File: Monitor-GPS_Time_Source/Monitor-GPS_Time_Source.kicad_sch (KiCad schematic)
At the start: 17 parts, among them J1 Conn_ARM_JTAG_SWD_10, J2 Conn_01x10_Pin, J3 Conn_01x10_Pin, J4 Conn_01x03_Pin, SW2 SW_Push, U1 MSPM0C1105, U2 BL8565

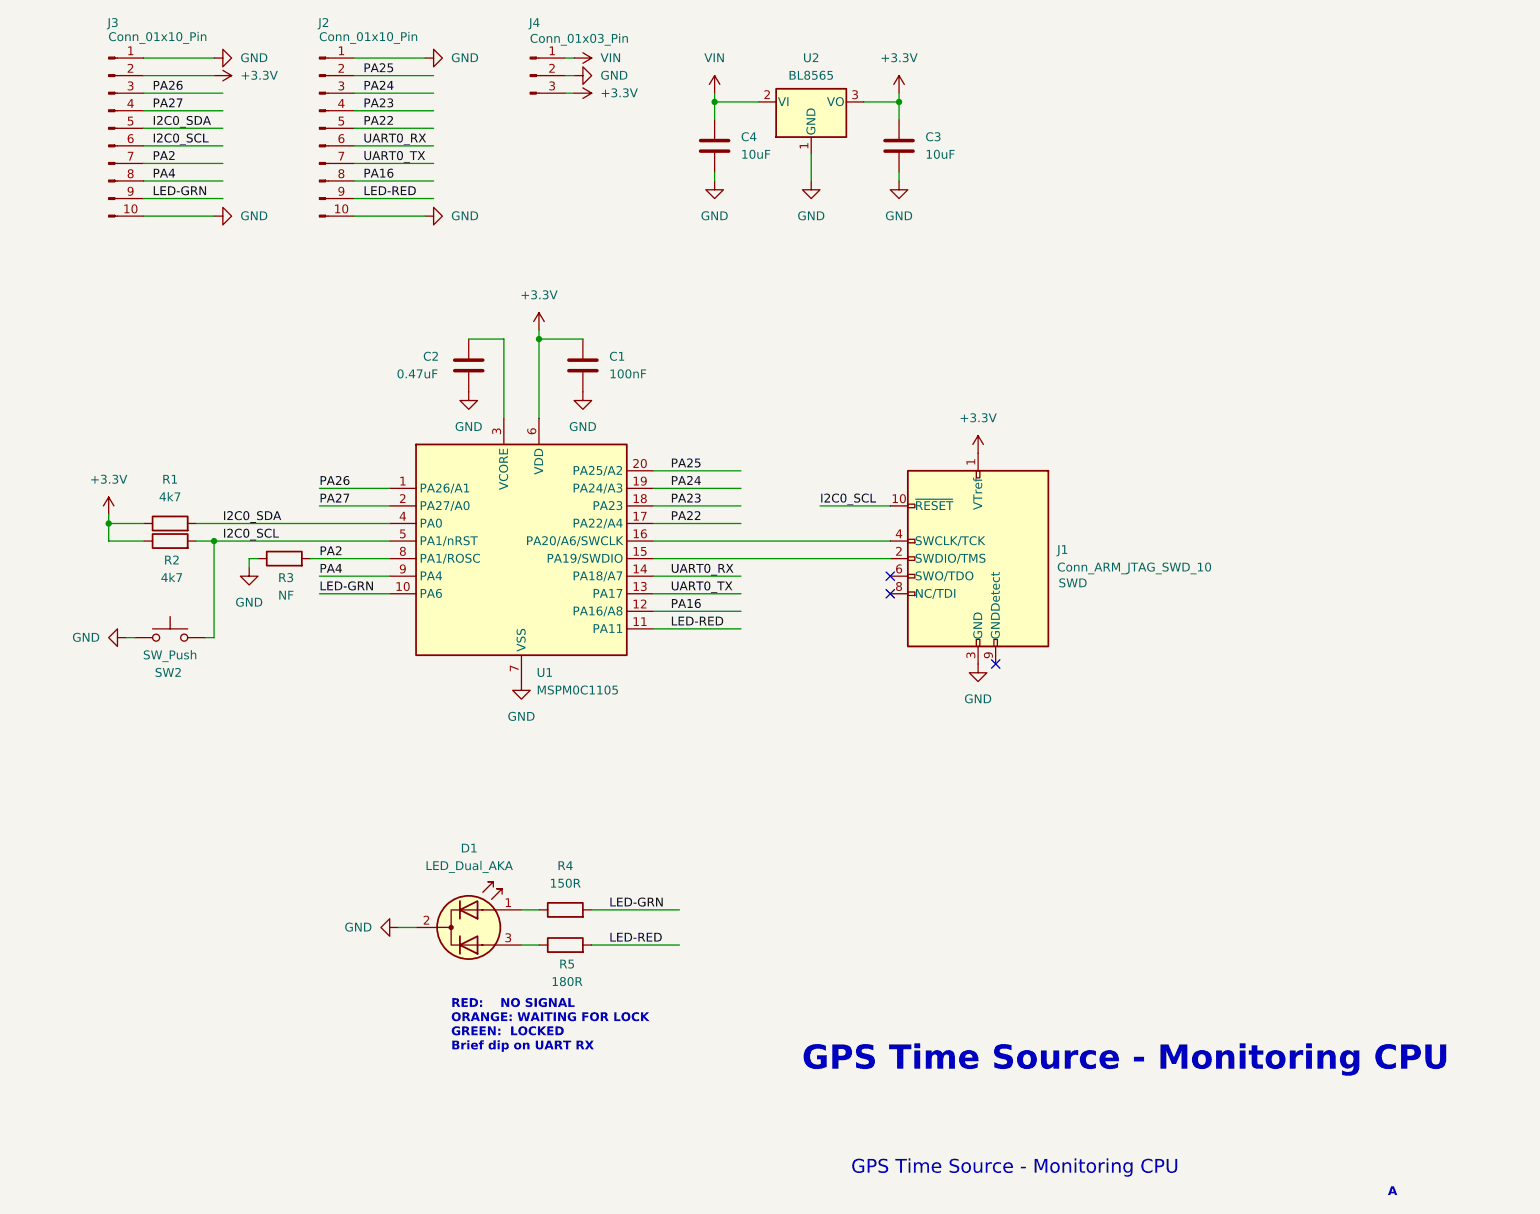
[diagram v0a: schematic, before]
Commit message: Add silkscreen text. Update sch to support MSPM0C110x
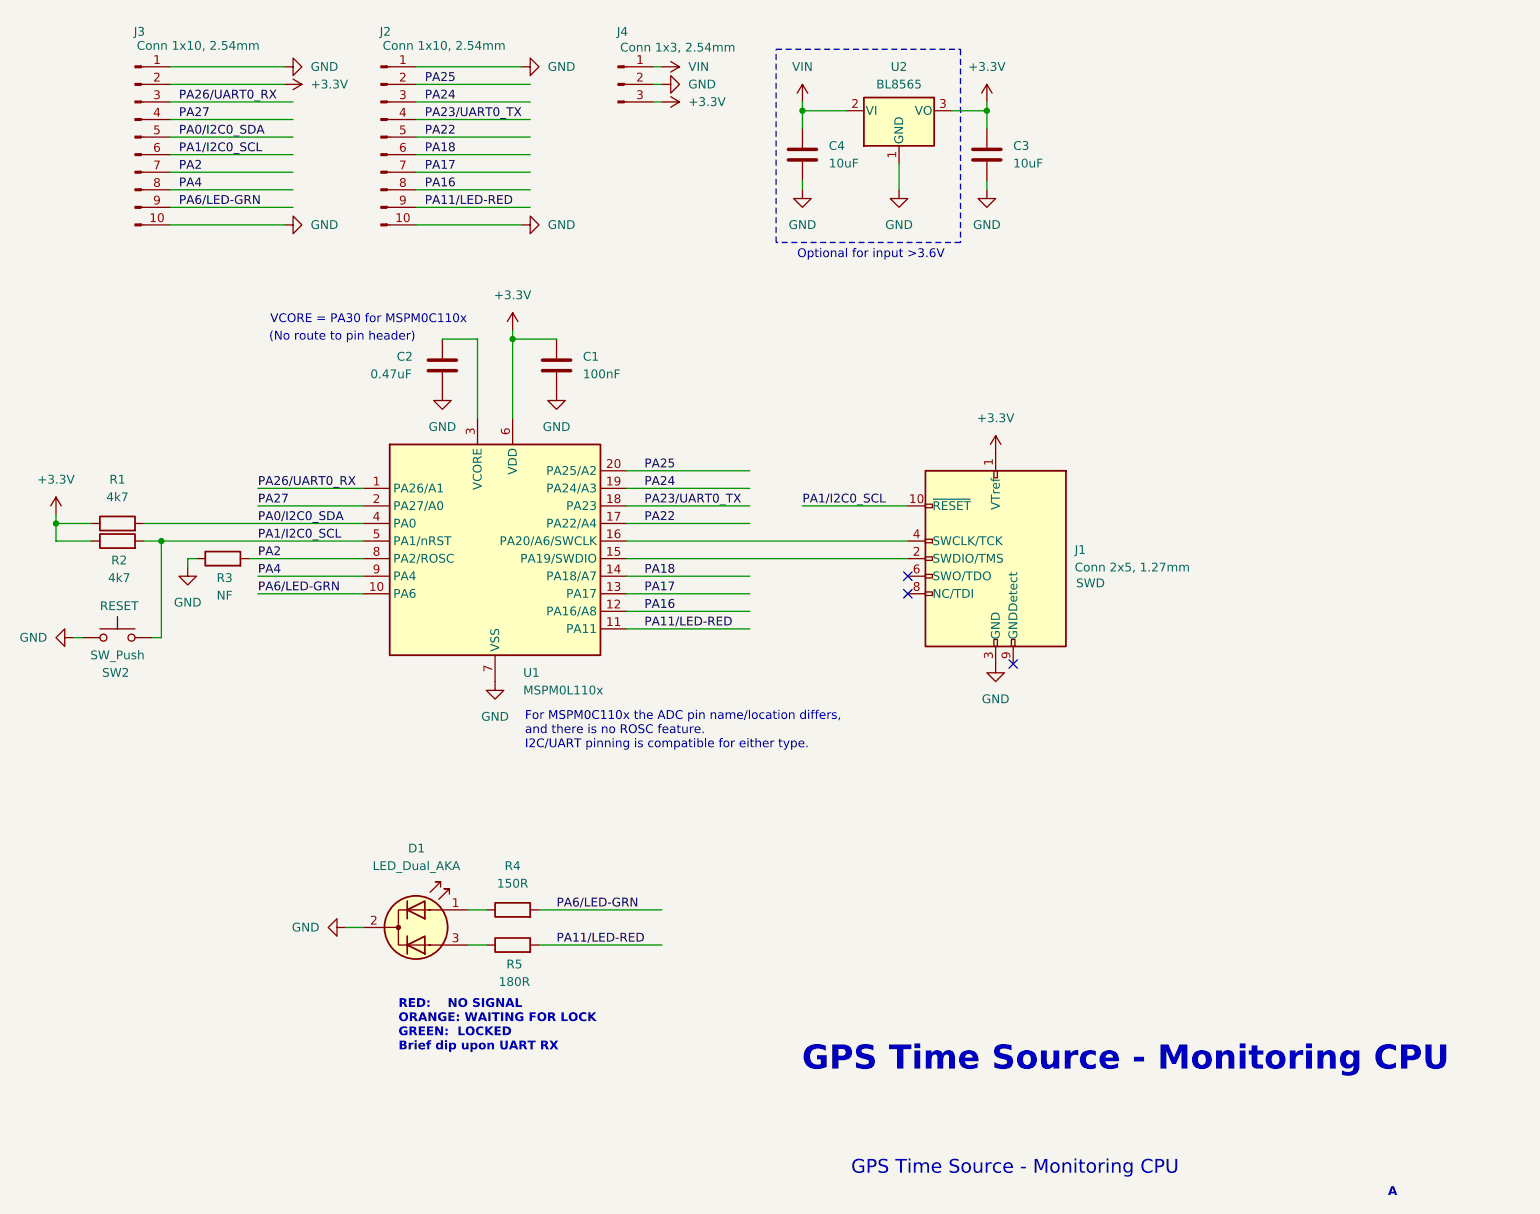
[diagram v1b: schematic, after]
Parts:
- J1: value Conn_ARM_JTAG_SWD_10 -> Conn 2x5, 1.27mm
- J2, J3: value Conn_01x10_Pin -> Conn 1x10, 2.54mm
- J4: value Conn_01x03_Pin -> Conn 1x3, 2.54mm
- U1: value MSPM0C1105 -> MSPM0L110x
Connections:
- net I2C0_SCL renamed PA1/I2C0_SCL
- net I2C0_SDA renamed PA0/I2C0_SDA
- net LED-GRN renamed PA6/LED-GRN
- net LED-RED renamed PA11/LED-RED
- net PA23 renamed PA23/UART0_TX
- net PA26 renamed PA26/UART0_RX
- net UART0_RX renamed PA18
- net UART0_TX renamed PA17
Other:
- note added: "(No route to pin header)"
- note added: "For MSPM0C110x the ADC pin name/location differs, and there is no ROSC feature. I2C/UART pinning is compatible for either type."
- note added: "Optional for input >3.6V"
- note added: "RED: NO SIGNAL ORANGE: WAITING FOR LOCK GREEN: LOCKED Brief dip upon UART RX"
- note added: "VCORE = PA30 for MSPM0C110x"
- note removed: "RED: NO SIGNAL ORANGE: WAITING FOR LOCK GREEN: LOCKED Brief dip on UART RX"
- moved on the sheet: C1, C2, C3, C4, D1, J1, J2, J3, J4, R1, R2, R3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
